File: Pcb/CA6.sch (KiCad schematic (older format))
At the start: 185 parts, among them J1 MICRO_USB, J2 BAT_CON, J3 MODULE_0, J4 MODULE_2, J5 MODULE_1, J6 AUX, J8 MODULE_3, P1 JTAG, P2 Connection_Card, P3 ESP-Programming-FTDI, Q1 BSS138P, Q10 BSS138P, Q11 BSS138P, Q12 BSS138P, Q13 BSS138P, Q14 BSS138P, Q15 BSS138P, Q16 BSS138P, Q2 BSS138P, Q3 BSS138P, Q4 BSS138P, Q5 BSS138P, Q6 BSS138P, Q7 BSS138P, Q8 BSS138P, Q9 BSS138P, SW1 ERASE, SW2 USB/BATTERY, SW3 RESET, SW4 BUTTON_0, U1 74LS244, U12 VREG_33, U16 ATSAM3X8EA-AU_LQFP-144, U2 74LS244, U3 SN74AHC1G08, U4 ESP-12E/F, X1 HOLE, X2 HOLE, X3 HOLE, X4 HOLE, X5 HOLE, X7 CRYSTAL_4, X8 32khz

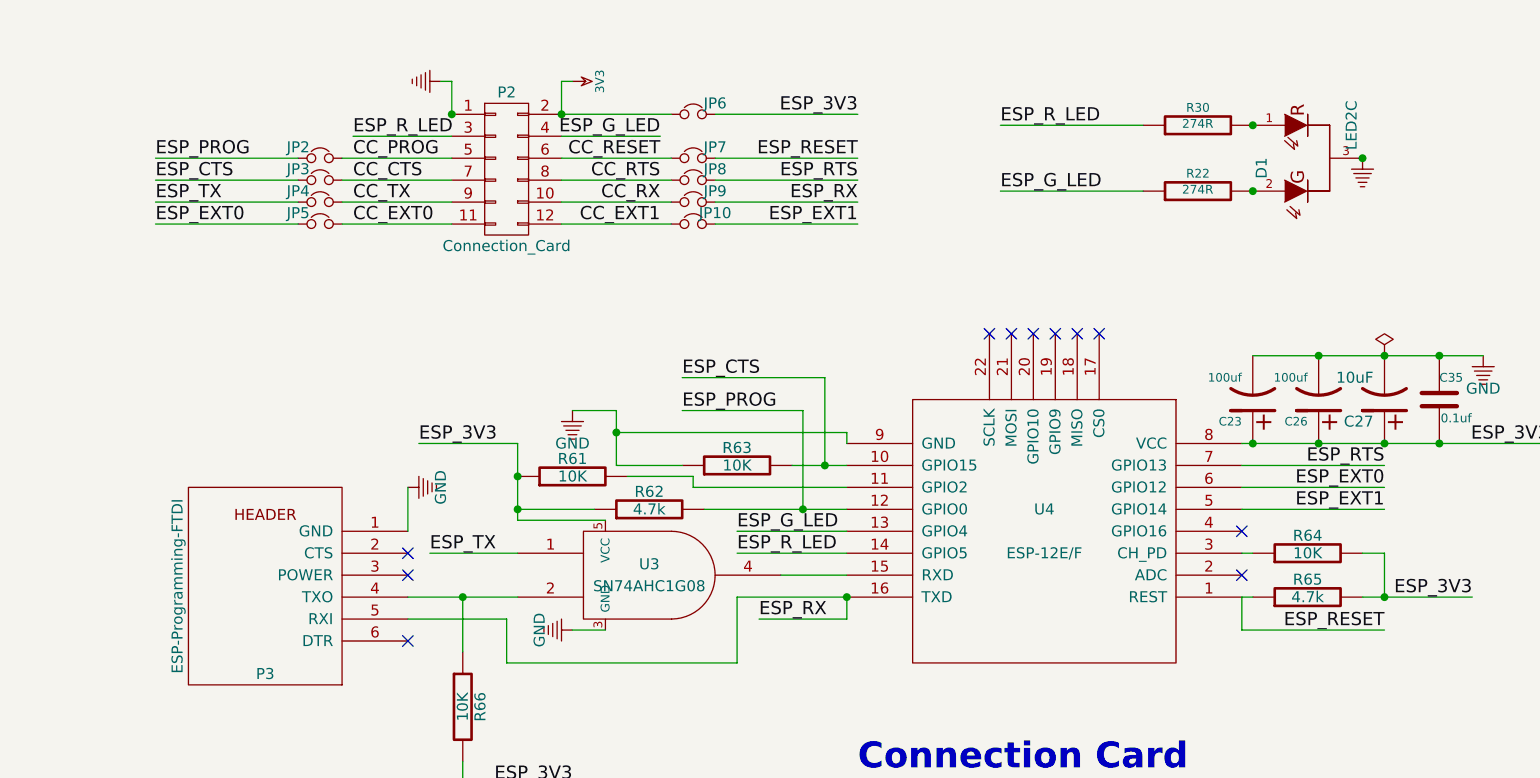
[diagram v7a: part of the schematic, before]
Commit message: Corrected labels in CA6.sch in the ESP & CC section.
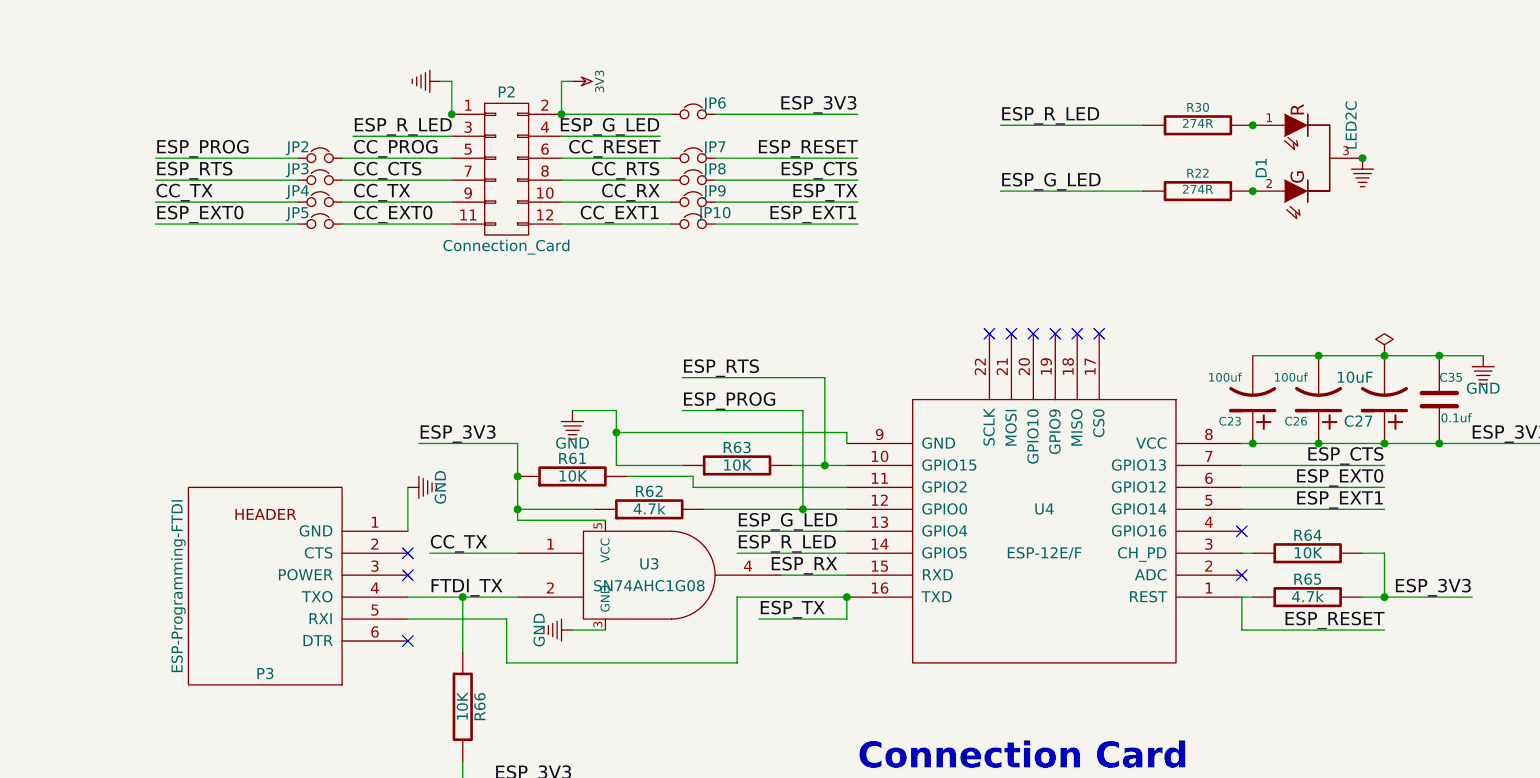
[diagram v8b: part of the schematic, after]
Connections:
- net CC_TX: now also JP4.1, U3.1
- net ESP_CTS: now also JP8.2, U4.7 (GPIO13); no longer JP3.1, R63.2, U4.10 (GPIO15)
- net ESP_RTS: now also JP3.1, R63.2, U4.10 (GPIO15); no longer JP8.2, U4.7 (GPIO13)
- net ESP_RX: no longer JP9.2, P3.5 (RXI), U4.16 (TXD)
- net ESP_TX: now also JP9.2, P3.5 (RXI), U4.16 (TXD); no longer JP4.1, U3.1
- net FTDI_TX: now reaches P3.4 (TXO), R66.1, U3.2
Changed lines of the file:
@@
 ESP_RESET
 Text Label 19550 11900 2    60   ~ 0
-ESP_RTS
+ESP_CTS
 Text Label 19550 12000 2    60   ~ 0
-ESP_RX
+ESP_TX
 Text Label 19550 12100 2    60   ~ 0
 ESP_EXT1
@@
 ESP_PROG
 Text Label 16350 11900 0    60   ~ 0
-ESP_CTS
+ESP_RTS
 Text Label 16350 12000 0    60   ~ 0
-ESP_TX
+CC_TX
 Text Label 16350 12100 0    60   ~ 0
 ESP_EXT0
@@
 ESP_EXT0
 Text Label 21950 13200 2    60   ~ 0
-ESP_RTS
+ESP_CTS
 Text Label 17600 13600 0    60   ~ 0
-ESP_TX
+CC_TX
 Wire Wire Line
 	18000 13600 17600 13600
@@
 Connection ~ 16700 6550
 Text Label 19100 13900 0    60   ~ 0
-ESP_RX
+ESP_TX
 Wire Wire Line
 	17500 13500 17500 13300
@@
 	19400 12800 18750 12800
 Text Label 18750 12800 0    60   ~ 0
-ESP_CTS
+ESP_RTS
 Wire Wire Line
 	18450 13200 18750 13200
@@
 Connection ~ 22200 13100
 Connection ~ 22200 12700
+Text Label 19150 13700 0    60   ~ 0
+ESP_RX
+Text Label 17600 13800 0    60   ~ 0
+FTDI_TX
 $EndSCHEMATC
